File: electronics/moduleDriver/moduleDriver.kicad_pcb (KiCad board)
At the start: 2 copper layers, 100 x 100 mm, 89 parts, among them J1 Power In, J11 Motor A, J12 Motor E, J13 Motor I, J14 Motor B, J15 Motor F, J16 Motor J, J17 Motor C, J18 Motor G, J19 Motor K, J2 UART, J20 Motor D, J21 Motor H, J22 Motor L, J3 SENSOR, J4 IOVCC, J5 GND, J6 SR CHAIN IN, J7 SR CHAIN OUT, Q1 BSS138, Q2 BSS138, U1 Mega2560Shield, U10 ULN2003AModule, U11 INA219 Breakout Wide (blue), U12 ULN2003AModule, U13 ULN2003AModule, U14 ULN2003AModule, U15 ULN2003AModule, U16 LevelShifterModule, U17 RS485Module, U18 TTGO_TDisplay, U19 74HC244, U2 SSD1306_I2C, U20 74HC165, U21 74HC165, U22 ST7789_80x160, U23 D1_32, U24 74HC595, U25 74HC595, U26 74HC595, U27 74HC595, U28 74HC595, U29 74HC595, U3 ULN2003AModule, U30 ST7789_240x240, U31 INA219 Breakout Narrow (purpl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, U32 SP485, U33 INA219BxD, U34 TPL7407LA, U35 TPL7407LA, U36 TPL7407LA, U37 TPL7407LA, U38 TPL7407LA, U39 TPL7407LA, U4 ULN2003AModule, U40 TPL7407LA, U5 ULN2003AModule, U6 ULN2003AModule, U7 ULN2003AModule, U8 ULN2003AModule, U9 ULN2003AModule

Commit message: Checkpoint
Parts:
- removed J11: Motor A, JST_XH_Connectors:JST_XH_2-5mm_5pin
- removed J12: Motor E, JST_XH_Connectors:JST_XH_2-5mm_5pin
- removed J13: Motor I, JST_XH_Connectors:JST_XH_2-5mm_5pin
- removed J14: Motor B, JST_XH_Connectors:JST_XH_2-5mm_5pin
- removed J15: Motor F, JST_XH_Connectors:JST_XH_2-5mm_5pin
- removed J16: Motor J, JST_XH_Connectors:JST_XH_2-5mm_5pin
- removed J17: Motor C, JST_XH_Connectors:JST_XH_2-5mm_5pin
- removed J18: Motor G, JST_XH_Connectors:JST_XH_2-5mm_5pin
- removed J19: Motor K, JST_XH_Connectors:JST_XH_2-5mm_5pin
- removed J20: Motor D, JST_XH_Connectors:JST_XH_2-5mm_5pin
- removed J21: Motor H, JST_XH_Connectors:JST_XH_2-5mm_5pin
- removed J22: Motor L, JST_XH_Connectors:JST_XH_2-5mm_5pin
- removed J6: SR CHAIN IN, Connector_PinSocket_2.54mm:PinSocket_1x06_P2.54mm_Vertical
- removed J7: SR CHAIN OUT, Connector_PinSocket_2.54mm:PinSocket_1x06_P2.54mm_Vertical
- removed JP2: RX 3.3V, Jumper:SolderJumper-2_P1.3mm_Open_TrianglePad1.0x1.5mm
- removed JP3: TX 3.3V, Jumper:SolderJumper-2_P1.3mm_Open_TrianglePad1.0x1.5mm
- removed Q1, Q2: BSS138, Package_TO_SOT_SMD:SOT-23
- removed R1, R10, R11, R12, R2, R3, R4, R5, R6, R7, R8, R9: 47k, Resistor_THT:R_Axial_DIN0204_L3.6mm_D1.6mm_P1.90mm_Vertical
- removed R13, R14, R15, R16: 10k, Resistor_SMD:R_0805_2012Metric_Pad1.15x1.40mm_HandSolder
- removed U16: LevelShifterModule, LevelShifterModule:LevelShifterModule
- removed U18: TTGO_TDisplay, ESP32:T-DISPLAY
- removed U19: 74HC244, Package_DIP:DIP-20_W7.62mm
- removed U20, U21: 74HC165, Package_DIP:DIP-16_W7.62mm
- removed U22: ST7789_80x160, ST7789:ST7789_80x160
- removed U23: D1_32, ESP32:D1_32
- removed U24, U25, U26, U27, U28, U29: 74HC595, Package_DIP:DIP-16_W7.62mm
- removed U30: ST7789_240x240, ST7789:ST7789_240x240
- removed U34, U35, U36, U37, U38, U39, U40: TPL7407LA, Package_SO:SOIC-16_3.9x9.9mm_P1.27mm
- added C1: 0.1uF, Capacitor_SMD:C_0805_2012Metric_Pad1.15x1.40mm_HandSolder, F.Cu at (87.6, 88.9)
- added C10: 0.1uF, Capacitor_SMD:C_0805_2012Metric_Pad1.15x1.40mm_HandSolder, F.Cu at (114.9, 72.4)
- added C11: 0.1uF, Capacitor_SMD:C_0805_2012Metric_Pad1.15x1.40mm_HandSolder, F.Cu at (114.9, 52.1)
- added C12: 0.1uF, Capacitor_SMD:C_0805_2012Metric_Pad1.15x1.40mm_HandSolder, F.Cu at (114.9, 31.8)
- added C13: 0.1uF, Capacitor_SMD:C_0805_2012Metric_Pad1.15x1.40mm_HandSolder, F.Cu at (82.5, 24.8)
- added C14: 0.1uF, Capacitor_SMD:C_0805_2012Metric_Pad1.15x1.40mm_HandSolder, F.Cu at (62.2, 24.8)
- added C15: 0.1uF, Capacitor_SMD:C_0805_2012Metric_Pad1.15x1.40mm_HandSolder, F.Cu at (41.9, 24.8)
- added C16: 0.1uF, Capacitor_SMD:C_0805_2012Metric_Pad1.15x1.40mm_HandSolder, F.Cu at (22.9, 24.8)
- added C2: 0.1uF, Capacitor_SMD:C_0805_2012Metric_Pad1.15x1.40mm_HandSolder, F.Cu at (50.8, 55.2)
- added C3: 100uF, Capacitor_THT:CP_Radial_D10.0mm_P5.00mm_P7.50mm, F.Cu at (39.4, 78.7)
- added C4: 10uF, Capacitor_THT:CP_Radial_D10.0mm_P2.50mm_P5.00mm, F.Cu at (47.0, 87.6)
- added C5: 0.1uF, Capacitor_SMD:C_0805_2012Metric_Pad1.15x1.40mm_HandSolder, F.Cu at (36.8, 114.9)
- added C6: 0.1uF, Capacitor_SMD:C_0805_2012Metric_Pad1.15x1.40mm_HandSolder, F.Cu at (57.1, 114.9)
- added C7: 0.1uF, Capacitor_SMD:C_0805_2012Metric_Pad1.15x1.40mm_HandSolder, F.Cu at (77.5, 114.9)
- added C8: 0.1uF, Capacitor_SMD:C_0805_2012Metric_Pad1.15x1.40mm_HandSolder, F.Cu at (97.8, 114.9)
- added C9: 0.1uF, Capacitor_SMD:C_0805_2012Metric_Pad1.15x1.40mm_HandSolder, F.Cu at (114.9, 92.7)
- added D1: SK6812_A, LED_SMD:LED_SK6812_PLCC4_5.0x5.0mm_P3.2mm, F.Cu at (29.2, 113.7)
- added D10: SK6812_J, LED_SMD:LED_SK6812_PLCC4_5.0x5.0mm_P3.2mm, F.Cu at (69.8, 26.0)
- added D11: SK6812_K, LED_SMD:LED_SK6812_PLCC4_5.0x5.0mm_P3.2mm, F.Cu at (49.5, 26.0)
- added D12: SK6812_L, LED_SMD:LED_SK6812_PLCC4_5.0x5.0mm_P3.2mm, F.Cu at (29.2, 26.0)
- added D2: SK6812_B, LED_SMD:LED_SK6812_PLCC4_5.0x5.0mm_P3.2mm, F.Cu at (49.5, 113.7)
- added D3: SK6812_C, LED_SMD:LED_SK6812_PLCC4_5.0x5.0mm_P3.2mm, F.Cu at (69.8, 113.7)
- added D4: SK6812_D, LED_SMD:LED_SK6812_PLCC4_5.0x5.0mm_P3.2mm, F.Cu at (90.2, 113.7)
- added D5: SK6812_E, LED_SMD:LED_SK6812_PLCC4_5.0x5.0mm_P3.2mm, F.Cu at (113.7, 100.3)
- added D6: SK6812_F, LED_SMD:LED_SK6812_PLCC4_5.0x5.0mm_P3.2mm, F.Cu at (113.7, 80.0)
- added D7: SK6812_G, LED_SMD:LED_SK6812_PLCC4_5.0x5.0mm_P3.2mm, F.Cu at (113.7, 59.7)
- added D8: SK6812_H, LED_SMD:LED_SK6812_PLCC4_5.0x5.0mm_P3.2mm, F.Cu at (113.7, 39.4)
- added D9: SK6812_I, LED_SMD:LED_SK6812_PLCC4_5.0x5.0mm_P3.2mm, F.Cu at (90.2, 26.0)
- added J10: 12V SENSE, TerminalBlock:TerminalBlock_bornier-2_P5.08mm, F.Cu at (29.8, 55.9)
- added J8: RS485, TerminalBlock:TerminalBlock_bornier-2_P5.08mm, F.Cu at (80.0, 73.7)
- added J9: RS485, TerminalBlock:TerminalBlock_bornier-2_P5.08mm, F.Cu at (80.0, 83.8)
- J4: value IOVCC -> 5V
- U10: value ULN2003AModule -> ULN2003A_E; footprint ULN2003AModule:ULN2003AModule -> ULN2003AModule:ULN2003AModule_No_EN
- U12: value ULN2003AModule -> ULN2003A_D; footprint ULN2003AModule:ULN2003AModule -> ULN2003AModule:ULN2003AModule_No_EN
- U13: value ULN2003AModule -> ULN2003A_C; footprint ULN2003AModule:ULN2003AModule -> ULN2003AModule:ULN2003AModule_No_EN
- U14: value ULN2003AModule -> ULN2003A_B; footprint ULN2003AModule:ULN2003AModule -> ULN2003AModule:ULN2003AModule_No_EN
- U15: value ULN2003AModule -> ULN2003A_A; footprint ULN2003AModule:ULN2003AModule -> ULN2003AModule:ULN2003AModule_No_EN
- U2: footprint Connector_PinSocket_2.54mm:PinSocket_1x04_P2.54mm_Vertical -> SSD1306:SSD1306_128x32
- U3: value ULN2003AModule -> ULN2003A_L; footprint ULN2003AModule:ULN2003AModule -> ULN2003AModule:ULN2003AModule_No_EN
- U4: value ULN2003AModule -> ULN2003A_K; footprint ULN2003AModule:ULN2003AModule -> ULN2003AModule:ULN2003AModule_No_EN
- U5: value ULN2003AModule -> ULN2003A_J; footprint ULN2003AModule:ULN2003AModule -> ULN2003AModule:ULN2003AModule_No_EN
- U6: value ULN2003AModule -> ULN2003A_I; footprint ULN2003AModule:ULN2003AModule -> ULN2003AModule:ULN2003AModule_No_EN
- U7: value ULN2003AModule -> ULN2003A_H; footprint ULN2003AModule:ULN2003AModule -> ULN2003AModule:ULN2003AModule_No_EN
- U8: value ULN2003AModule -> ULN2003A_G; footprint ULN2003AModule:ULN2003AModule -> ULN2003AModule:ULN2003AModule_No_EN
- U9: value ULN2003AModule -> ULN2003A_F; footprint ULN2003AModule:ULN2003AModule -> ULN2003AModule:ULN2003AModule_No_EN
- moved J2 380.4 mm to (29.8, 78.7), turned to 270 degrees
- moved JP5 363.7 mm to (49.2, 64.9)
- moved JP4 363.7 mm to (53.5, 64.9)
- moved J1 354.0 mm to (29.8, 62.2), turned to 270 degrees
- moved H1 336.9 mm to (24.0, 37.5)
- moved U33 315.3 mm to (50.8, 59.7), turned to 180 degrees
- moved H3 306.9 mm to (24.0, 102.5)
- moved U32 301.3 mm to (88.9, 83.8), turned to 180 degrees
- moved H2 284.1 mm to (116.0, 116.1)
- moved R17 223.9 mm to (53.3, 69.8), turned to 270 degrees
- moved H4 211.9 mm to (115.8, 24.1)
- moved R18 210.3 mm to (49.5, 69.8), turned to 270 degrees
- moved U17 191.1 mm to (96.5, 87.6), turned to 180 degrees
- moved R19 171.7 mm to (43.2, 61.0), turned to 90 degrees
- moved U2 157.4 mm to (64.8, 61.0)
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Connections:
- J4 pad 1: IOVCC -> +5V
- J4 pad 10: IOVCC -> +5V
- J4 pad 11: IOVCC -> +5V
- J4 pad 12: IOVCC -> +5V
- J4 pad 2: IOVCC -> +5V
- J4 pad 3: IOVCC -> +5V
- J4 pad 4: IOVCC -> +5V
- J4 pad 5: IOVCC -> +5V
- J4 pad 6: IOVCC -> +5V
- J4 pad 7: IOVCC -> +5V
- J4 pad 8: IOVCC -> +5V
- J4 pad 9: IOVCC -> +5V
- JP4 pad 1: IOVCC -> +5V
- JP5 pad 1: IOVCC -> +5V
- U1 pad A0: /MOTOR_A_PHASE_A -> /MOTOR_L_PHASE_D
- U1 pad A1: /MOTOR_A_PHASE_B -> /MOTOR_L_PHASE_C
- U1 pad A10: /MOTOR_C_PHASE_C -> /MOTOR_J_PHASE_B
- U1 pad A11: /MOTOR_C_PHASE_D -> /MOTOR_J_PHASE_A
- U1 pad A12: /MOTOR_D_PHASE_A -> /MOTOR_I_PHASE_D
- U1 pad A13: /MOTOR_D_PHASE_B -> /MOTOR_I_PHASE_C
- U1 pad A14: /MOTOR_D_PHASE_C -> /MOTOR_I_PHASE_B
- U1 pad A15: /MOTOR_D_PHASE_D -> /MOTOR_I_PHASE_A
- U1 pad A2: /MOTOR_A_PHASE_C -> /MOTOR_L_PHASE_B
- U1 pad A3: /MOTOR_A_PHASE_D -> /MOTOR_L_PHASE_A
- U1 pad A4: /MOTOR_B_PHASE_A -> /MOTOR_K_PHASE_D
- U1 pad A5: /MOTOR_B_PHASE_B -> /MOTOR_K_PHASE_C
- U1 pad A6: /MOTOR_B_PHASE_C -> /MOTOR_K_PHASE_B
- U1 pad A7: /MOTOR_B_PHASE_D -> /MOTOR_K_PHASE_A
- U1 pad A8: /MOTOR_C_PHASE_A -> /MOTOR_J_PHASE_D
- U1 pad A9: /MOTOR_C_PHASE_B -> /MOTOR_J_PHASE_C
- U1 pad D10: /MOTOR_L_PHASE_A -> /MOTOR_A_PHASE_D
- U1 pad D11: /MOTOR_L_PHASE_B -> /MOTOR_A_PHASE_C
- U1 pad D12: /MOTOR_L_PHASE_C -> /MOTOR_A_PHASE_B
- U1 pad D13: /MOTOR_L_PHASE_D -> /MOTOR_A_PHASE_A
- U1 pad D22: /MOTOR_K_PHASE_D -> /MOTOR_B_PHASE_D
- U1 pad D23: /MOTOR_K_PHASE_C -> /MOTOR_B_PHASE_C
- U1 pad D24: /MOTOR_K_PHASE_B -> /MOTOR_B_PHASE_B
- U1 pad D25: /MOTOR_K_PHASE_A -> /MOTOR_B_PHASE_A
- U1 pad D26: /MOTOR_J_PHASE_D -> /MOTOR_C_PHASE_D
- U1 pad D27: /MOTOR_J_PHASE_C -> /MOTOR_C_PHASE_C
- U1 pad D28: /MOTOR_J_PHASE_B -> /MOTOR_C_PHASE_B
- U1 pad D29: /MOTOR_J_PHASE_A -> /MOTOR_C_PHASE_A
- U1 pad D30: /MOTOR_I_PHASE_D -> /MOTOR_D_PHASE_A
- U1 pad D31: /MOTOR_I_PHASE_C -> /MOTOR_D_PHASE_B
- U1 pad D32: /MOTOR_I_PHASE_B -> /MOTOR_D_PHASE_C
- U1 pad D33: /MOTOR_I_PHASE_A -> /MOTOR_D_PHASE_D
- U1 pad D34: /MOTOR_H_PHASE_D -> /MOTOR_E_PHASE_A
- U1 pad D35: /MOTOR_H_PHASE_C -> /MOTOR_E_PHASE_B
- U1 pad D36: /MOTOR_H_PHASE_B -> /MOTOR_E_PHASE_C
- U1 pad D37: /MOTOR_H_PHASE_A -> /MOTOR_E_PHASE_D
- U1 pad D42: /MOTOR_G_PHASE_D -> /MOTOR_F_PHASE_A
- U1 pad D43: /MOTOR_G_PHASE_C -> /MOTOR_F_PHASE_B
- U1 pad D44: /MOTOR_G_PHASE_B -> /MOTOR_F_PHASE_C
- U1 pad D45: /MOTOR_G_PHASE_A -> /MOTOR_F_PHASE_D
- U1 pad D46: /MOTOR_F_PHASE_D -> /MOTOR_G_PHASE_A
- U1 pad D47: /MOTOR_F_PHASE_C -> /MOTOR_G_PHASE_B
- U1 pad D48: /MOTOR_F_PHASE_B -> /MOTOR_G_PHASE_C
- U1 pad D49: /MOTOR_F_PHASE_A -> /MOTOR_G_PHASE_D
- U1 pad D5: (no net) -> /LED_SIGNAL
- U1 pad D50: /MOTOR_E_PHASE_D -> /MOTOR_H_PHASE_A
- U1 pad D51: /MOTOR_E_PHASE_C -> /MOTOR_H_PHASE_B
- U1 pad D52: /MOTOR_E_PHASE_B -> /MOTOR_H_PHASE_C
- U1 pad D53: /MOTOR_E_PHASE_A -> /MOTOR_H_PHASE_D
- U1 pad IOREF: IOVCC -> (no net)
- U10 pad IN1: /MOTOR_H_PHASE_A -> /MOTOR_E_PHASE_A
- U10 pad IN2: /MOTOR_H_PHASE_B -> /MOTOR_E_PHASE_B
- U10 pad IN3: /MOTOR_H_PHASE_C -> /MOTOR_E_PHASE_C
- U10 pad IN4: /MOTOR_H_PHASE_D -> /MOTOR_E_PHASE_D
- U11 pad GND: (no net) -> GND
- U11 pad SCL: (no net) -> /SCL
- U11 pad SDA: (no net) -> /SDA
- U11 pad VCC: (no net) -> +5V
- U12 pad IN1: /MOTOR_I_PHASE_A -> /MOTOR_D_PHASE_A
- U12 pad IN2: /MOTOR_I_PHASE_B -> /MOTOR_D_PHASE_B
- U12 pad IN3: /MOTOR_I_PHASE_C -> /MOTOR_D_PHASE_C
- U12 pad IN4: /MOTOR_I_PHASE_D -> /MOTOR_D_PHASE_D
- U13 pad IN1: /MOTOR_J_PHASE_A -> /MOTOR_C_PHASE_A
- U13 pad IN2: /MOTOR_J_PHASE_B -> /MOTOR_C_PHASE_B
- U13 pad IN3: /MOTOR_J_PHASE_C -> /MOTOR_C_PHASE_C
- U13 pad IN4: /MOTOR_J_PHASE_D -> /MOTOR_C_PHASE_D
- U14 pad IN1: /MOTOR_K_PHASE_A -> /MOTOR_B_PHASE_A
- U14 pad IN2: /MOTOR_K_PHASE_B -> /MOTOR_B_PHASE_B
- U14 pad IN3: /MOTOR_K_PHASE_C -> /MOTOR_B_PHASE_C
- U14 pad IN4: /MOTOR_K_PHASE_D -> /MOTOR_B_PHASE_D
- U15 pad IN1: /MOTOR_L_PHASE_A -> /MOTOR_A_PHASE_A
- U15 pad IN2: /MOTOR_L_PHASE_B -> /MOTOR_A_PHASE_B
- U15 pad IN3: /MOTOR_L_PHASE_C -> /MOTOR_A_PHASE_C
- U15 pad IN4: /MOTOR_L_PHASE_D -> /MOTOR_A_PHASE_D
- U2 pad 3: IOVCC -> +5V
- U3 pad IN1: /MOTOR_A_PHASE_A -> /MOTOR_L_PHASE_A
- U3 pad IN2: /MOTOR_A_PHASE_B -> /MOTOR_L_PHASE_B
- U3 pad IN3: /MOTOR_A_PHASE_C -> /MOTOR_L_PHASE_C
- U3 pad IN4: /MOTOR_A_PHASE_D -> /MOTOR_L_PHASE_D
- U31 pad GND: (no net) -> GND
- U31 pad SCL: (no net) -> /SCL
- U31 pad SDA: (no net) -> /SDA
- U31 pad VCC: (no net) -> +5V
- U32 pad 6: (no net) -> /RS485_A
- U32 pad 7: (no net) -> /RS485_B
- U33 pad 5: IOVCC -> +5V
- U4 pad IN1: /MOTOR_B_PHASE_A -> /MOTOR_K_PHASE_A
- U4 pad IN2: /MOTOR_B_PHASE_B -> /MOTOR_K_PHASE_B
- U4 pad IN3: /MOTOR_B_PHASE_C -> /MOTOR_K_PHASE_C
- U4 pad IN4: /MOTOR_B_PHASE_D -> /MOTOR_K_PHASE_D
- U5 pad IN1: /MOTOR_C_PHASE_A -> /MOTOR_J_PHASE_A
- U5 pad IN2: /MOTOR_C_PHASE_B -> /MOTOR_J_PHASE_B
- U5 pad IN3: /MOTOR_C_PHASE_C -> /MOTOR_J_PHASE_C
- U5 pad IN4: /MOTOR_C_PHASE_D -> /MOTOR_J_PHASE_D
- U6 pad IN1: /MOTOR_D_PHASE_A -> /MOTOR_I_PHASE_A
- U6 pad IN2: /MOTOR_D_PHASE_B -> /MOTOR_I_PHASE_B
- U6 pad IN3: /MOTOR_D_PHASE_C -> /MOTOR_I_PHASE_C
- U6 pad IN4: /MOTOR_D_PHASE_D -> /MOTOR_I_PHASE_D
- U7 pad IN1: /MOTOR_E_PHASE_A -> /MOTOR_H_PHASE_A
- U7 pad IN2: /MOTOR_E_PHASE_B -> /MOTOR_H_PHASE_B
- U7 pad IN3: /MOTOR_E_PHASE_C -> /MOTOR_H_PHASE_C
- U7 pad IN4: /MOTOR_E_PHASE_D -> /MOTOR_H_PHASE_D
- U8 pad IN1: /MOTOR_F_PHASE_A -> /MOTOR_G_PHASE_A
- U8 pad IN2: /MOTOR_F_PHASE_B -> /MOTOR_G_PHASE_B
- U8 pad IN3: /MOTOR_F_PHASE_C -> /MOTOR_G_PHASE_C
- U8 pad IN4: /MOTOR_F_PHASE_D -> /MOTOR_G_PHASE_D
- U9 pad IN1: /MOTOR_G_PHASE_A -> /MOTOR_F_PHASE_A
- U9 pad IN2: /MOTOR_G_PHASE_B -> /MOTOR_F_PHASE_B
- U9 pad IN3: /MOTOR_G_PHASE_C -> /MOTOR_F_PHASE_C
- U9 pad IN4: /MOTOR_G_PHASE_D -> /MOTOR_F_PHASE_D
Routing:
- net +12V_Monitored: track 0.00 -> 406.8 mm
- net +5V: track 0.00 -> 296.8 mm, vias 0 -> 4
- net GND: track 0.00 -> 85.3 mm, vias 0 -> 10
- net /MOTOR_B_PHASE_A: track 0.00 -> 78.2 mm, vias 0 -> 1
- net /MOTOR_B_PHASE_B: track 0.00 -> 77.4 mm, vias 0 -> 1
- net /MOTOR_B_PHASE_C: track 0.00 -> 69.7 mm, vias 0 -> 1
- net /MOTOR_B_PHASE_D: track 0.00 -> 68.8 mm, vias 0 -> 1
- net /MOTOR_C_PHASE_B: track 0.00 -> 66.0 mm, vias 0 -> 1
- net /MOTOR_C_PHASE_A: track 0.00 -> 65.6 mm, vias 0 -> 1
- net /MOTOR_C_PHASE_C: track 0.00 -> 59.5 mm, vias 0 -> 1
- net /MOTOR_C_PHASE_D: track 0.00 -> 59.2 mm, vias 0 -> 1
- net /TX_EXT: track 0.00 -> 53.6 mm
- net /MOTOR_D_PHASE_A: track 0.00 -> 51.4 mm
- net /MOTOR_D_PHASE_C: track 0.00 -> 50.8 mm
- net /MOTOR_D_PHASE_B: track 0.00 -> 47.4 mm
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- added copper zone on B.Cu, net GND
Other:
- net class Default: clearance 0.2 -> 0.18; trace_width 0.25 -> 0.18
- net class Power added: clearance 0.75, trace_width 1.4, via_dia 0.8, via_drill 0.4
- rule trace_clearance: 0.2 -> 0.18
- rule trace_min: 0.2 -> 0.18
- board text added: "A"
- board text added: "B"
- board text added: "Splitflap Mega Direct v0.1"

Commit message: Initial routing
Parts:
- C3: footprint Capacitor_THT:CP_Radial_D10.0mm_P5.00mm_P7.50mm -> Capacitor_THT:CP_Radial_D10.0mm_P3.50mm
- C4: footprint Capacitor_THT:CP_Radial_D10.0mm_P2.50mm_P5.00mm -> Capacitor_THT:CP_Radial_D6.3mm_P2.50mm
- moved D1 88.4 mm to (34.3, 25.4)
- moved D2 88.4 mm to (54.6, 25.4)
- moved D3 88.4 mm to (74.9, 25.4)
- moved D4 88.4 mm to (95.2, 25.4)
- moved D10 88.4 mm to (74.9, 114.3)
- moved D11 88.4 mm to (54.6, 114.3)
- moved D12 88.4 mm to (34.3, 114.3)
- moved D9 88.4 mm to (95.2, 114.3)
- moved C13 87.8 mm to (88.3, 112.4)
- moved C14 87.8 mm to (67.9, 112.4)
- moved C16 87.8 mm to (27.9, 112.4)
- moved C6 87.7 mm to (61.6, 27.3)
- moved C7 87.7 mm to (81.9, 27.3)
- moved C8 87.7 mm to (102.2, 27.3)
- moved C15 87.2 mm to (48.3, 111.8)
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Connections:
- U1 pad D20: /SDA -> (no net)
- U1 pad D21: /SCL -> (no net)
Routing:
- net +5V: track 296.8 -> 568.1 mm, vias 4 -> 6
- net /RX_EXT: track 5.93 -> 127.7 mm, vias 0 -> 4
- net +12V: track 34.0 -> 105.5 mm
- net /TX_EXT: track 53.6 -> 120.8 mm, vias 0 -> 4
- net /RS485_DRIVE_EN: track 12.1 -> 68.0 mm
- net /LED_SIGNAL: track 0.00 -> 37.1 mm, vias 0 -> 2
- net /SCL: track 35.1 -> 53.9 mm
- net /SDA: track 30.8 -> 49.0 mm
- net /MOTOR_B_PHASE_D: track 68.8 -> 56.4 mm
- net /MOTOR_C_PHASE_D: track 59.2 -> 48.1 mm
- net /MOTOR_C_PHASE_C: track 59.5 -> 49.4 mm
- net /MOTOR_C_PHASE_B: track 66.0 -> 57.3 mm
- net /MOTOR_D_PHASE_C: track 50.8 -> 42.2 mm
- net /MOTOR_B_PHASE_C: track 69.7 -> 61.5 mm
- net /MOTOR_B_PHASE_B: track 77.4 -> 69.4 mm
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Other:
- net class 5V added: clearance 0.25, trace_width 0.3, via_dia 0.8, via_drill 0.4
- board text added: "12V"
- board text added: "5V"
- board text added: "Comms"
- board text added: "GND"
- board text added: "Power"
- board text added: "RX"
- board text added: "TX"
- board text added: "VIN+"
- board text added: "VIN-"
- board text removed: "Splitflap Mega Direct v0.1"

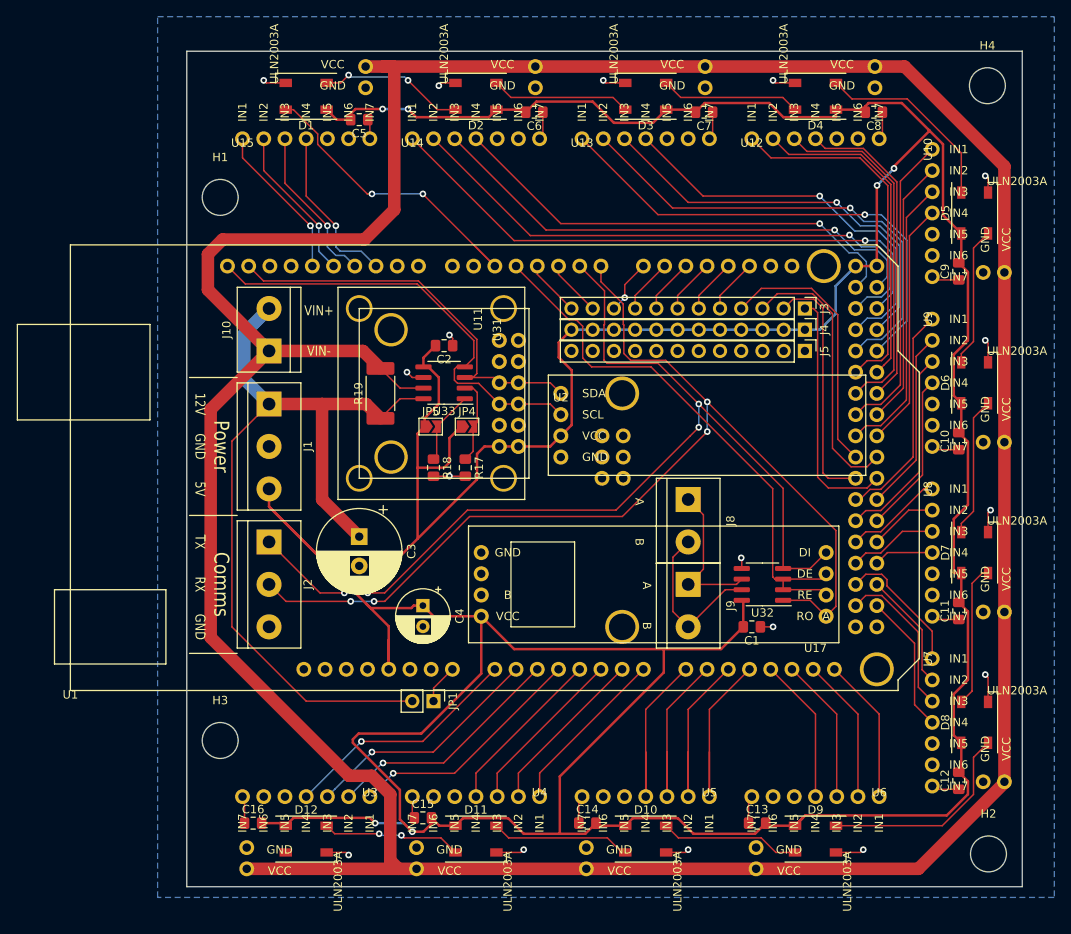
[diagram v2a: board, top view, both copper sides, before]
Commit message: Silkscreen cleanup
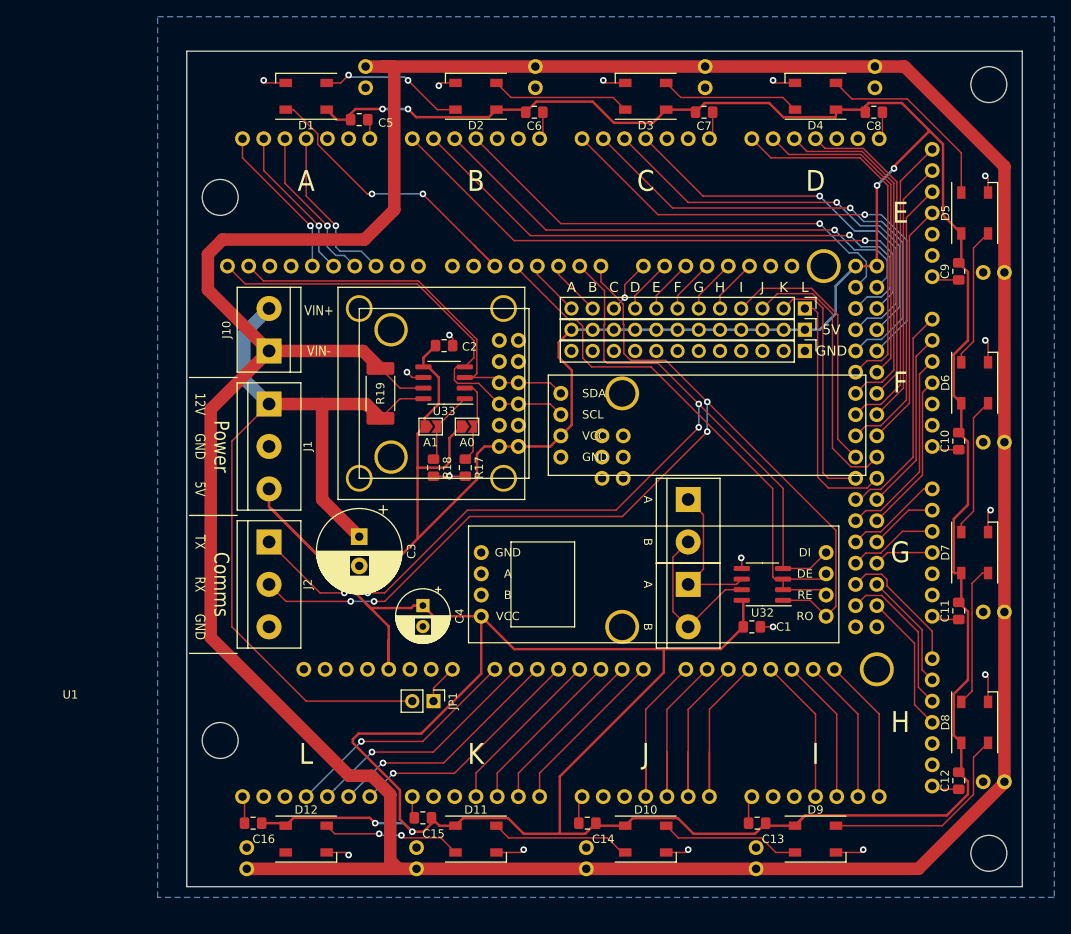
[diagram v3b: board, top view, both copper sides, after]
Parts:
- U1: footprint Mega2560Shield:Mega2560Shield -> Mega2560Shield:Mega2560Shield_Modified
- U10, U12, U13, U14, U15, U3, U4, U5, U6, U7, U8, U9: footprint ULN2003AModule:ULN2003AModule_No_EN -> ULN2003AModule:ULN2003AModule_No_EN_No_FSilk
- moved H4 0.22 mm to (116.0, 24.0)
- moved H2 0.09 mm to (116.0, 116.0)
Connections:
- J3 pad 1: /SENSOR_A -> /SENSOR_L
- J3 pad 10: /SENSOR_J -> /SENSOR_C
- J3 pad 11: /SENSOR_K -> /SENSOR_B
- J3 pad 12: /SENSOR_L -> /SENSOR_A
- J3 pad 2: /SENSOR_B -> /SENSOR_K
- J3 pad 3: /SENSOR_C -> /SENSOR_J
- J3 pad 4: /SENSOR_D -> /SENSOR_I
- J3 pad 5: /SENSOR_E -> /SENSOR_H
- J3 pad 6: /SENSOR_F -> /SENSOR_G
- J3 pad 7: /SENSOR_G -> /SENSOR_F
- J3 pad 8: /SENSOR_H -> /SENSOR_E
- J3 pad 9: /SENSOR_I -> /SENSOR_D
- U1 pad D14: /SENSOR_J -> /SENSOR_C
- U1 pad D15: /SENSOR_I -> /SENSOR_D
- U1 pad D16: /SENSOR_H -> /SENSOR_E
- U1 pad D17: /SENSOR_G -> /SENSOR_F
- U1 pad D18: /SENSOR_F -> /SENSOR_G
- U1 pad D19: /SENSOR_E -> /SENSOR_H
- U1 pad D2: /SENSOR_K -> /SENSOR_B
- U1 pad D3: /SENSOR_L -> /SENSOR_A
- U1 pad D38: /SENSOR_D -> /SENSOR_I
- U1 pad D39: /SENSOR_C -> /SENSOR_J
- U1 pad D40: /SENSOR_B -> /SENSOR_K
- U1 pad D41: /SENSOR_A -> /SENSOR_L
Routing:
- net /SENSOR_J: track 6.54 -> 32.9 mm, vias 1 -> 0
- net /SENSOR_C: track 32.9 -> 6.54 mm, vias 0 -> 1
- net /SENSOR_I: track 6.54 -> 31.8 mm
- net /SENSOR_D: track 31.8 -> 6.54 mm
- net /SENSOR_L: track 6.77 -> 29.5 mm
- net /SENSOR_A: track 29.5 -> 6.77 mm
- net /SENSOR_K: track 6.77 -> 29.5 mm
- net /SENSOR_B: track 29.5 -> 6.77 mm
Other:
- board text added: "C"
- board text added: "D"
- board text added: "E"
- board text added: "F"
- board text added: "G"
- board text added: "H"
- board text added: "I"
- board text added: "J"
- board text added: "K"
- board text added: "L"

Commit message: Minor tweaks
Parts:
- moved J10 5.71 mm to (24.1, 55.9)
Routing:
- net /MOTOR_J_PHASE_D: track 22.6 -> 17.2 mm
- net /MOTOR_J_PHASE_C: track 22.6 -> 17.2 mm
- net /MOTOR_J_PHASE_B: track 22.6 -> 17.2 mm
- net /MOTOR_J_PHASE_A: track 22.6 -> 17.2 mm
- net /SENSOR_K: track 29.5 -> 27.6 mm
- net +12V_Monitored: track 403.7 -> 405.3 mm
- net /SENSOR_L: track 29.5 -> 28.5 mm

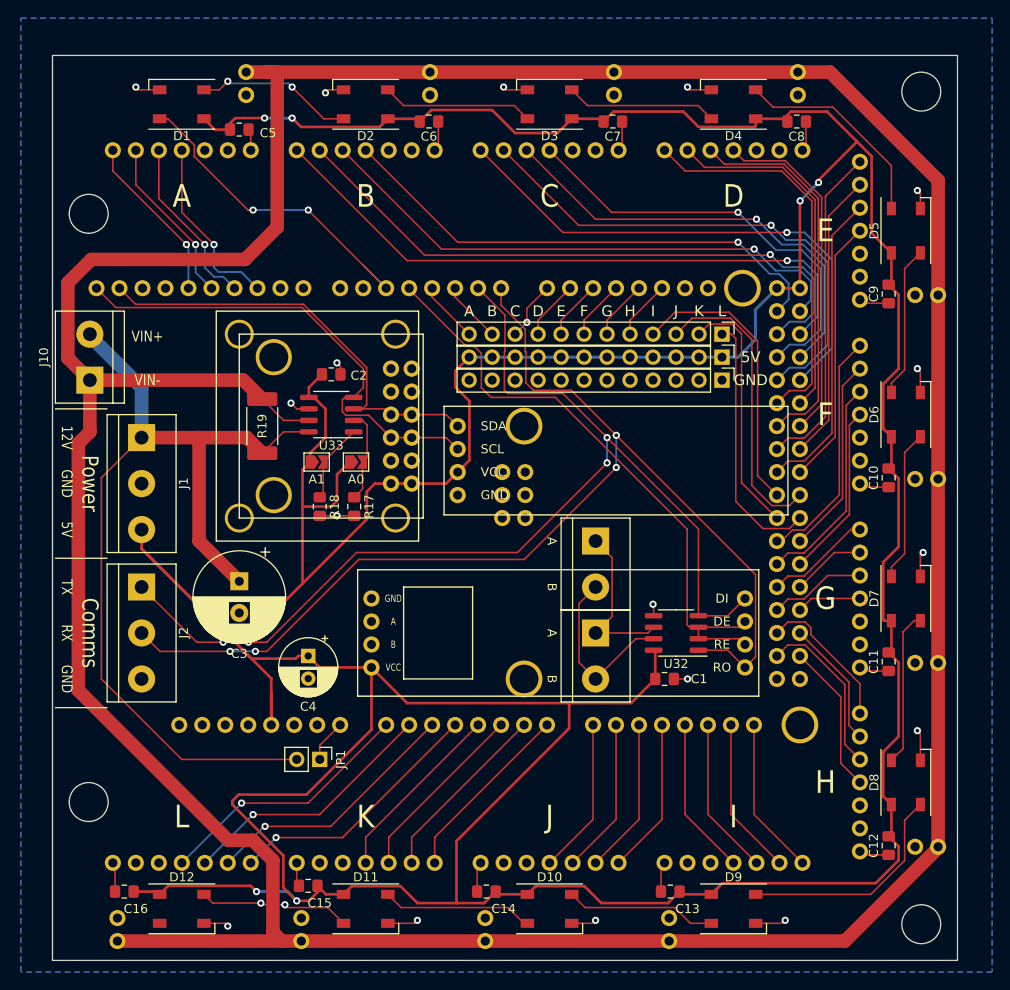
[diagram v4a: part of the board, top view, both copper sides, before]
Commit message: Change to plated holes
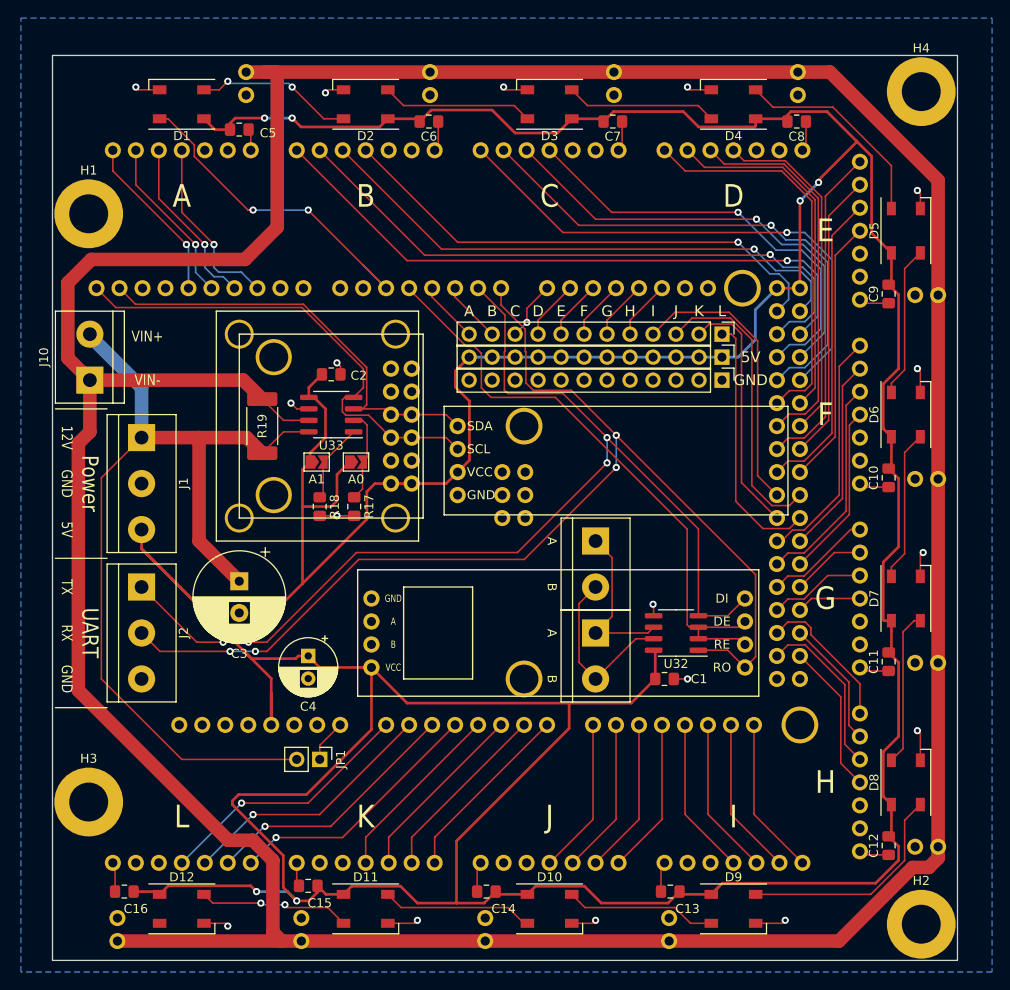
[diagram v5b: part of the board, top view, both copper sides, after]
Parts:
- H1, H2, H3, H4: footprint MountingHole:MountingHole_4.3mm_M4_ISO7380 -> MountingHole:MountingHole_4.3mm_M4_ISO7380_Pad
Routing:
- net +12V_Monitored: track 405.3 -> 406.0 mm
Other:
- board text added: "UART"
- board text removed: "Comms"

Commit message: Mega tweaks for alpha PCB order
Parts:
- moved J10 1.27 mm to (25.4, 55.9)
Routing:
- net +12V_Monitored: track 406.0 -> 404.7 mm
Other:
- rule pad_to_mask_clearance: 0.051 -> 0
- board text added: "Splitflap Mega Controller"
- board text added: "[alpha]"
